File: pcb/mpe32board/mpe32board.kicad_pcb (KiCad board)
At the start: 4 copper layers, 98 x 79 mm, 160 parts, among them J1 Conn_ST_STDC14, J10 Conn_01x04, J11 Conn_01x04, J12 Conn_01x04, J13 Conn_01x04, J14 Conn_01x04, J15 Conn_01x04, J16 Conn_01x04, J17 Conn_01x04, J18 Conn_01x04, J19 Conn_01x04, J2 USB_C_Receptacle_USB2.0_16P, J20 Conn_01x04, J21 Conn_01x04, J22 Conn_01x04, J23 Conn_01x04, J24 Conn_01x04, J25 Conn_01x04, J26 Conn_01x04, J27 Conn_01x04, J3 Conn_01x01_Socket, J4 Conn_01x04, J44 Conn_01x05, J45 Conn_01x04_Socket, J46 Conn_02x10_Counter_Clockwise, J48 Micro_SD_Card_Det_Hirose_DM3AT, J49 AudioJack3_SwitchT, J5 Conn_01x04, J6 Conn_01x04, J7 Conn_01x04, J8 Conn_01x04, J9 Conn_01x04, SW1 SW_Push, SW2 SW_Push, SW3 SW_Push, SW4 SW_Push, SW5 SW_Push, SW6 SW_Push, U1 TAC5212IRGER, U10 W9812G6KH-75, U11 IP4252CZ16, U2 USBLC6-2P6, U3 AMS1117-3.3, U4 TCA9548ARGER, U5 TCA9548ARGER, U6 TCA9548ARGER, U9 STM32H743IITx

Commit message: silkscreen connectors
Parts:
- added kibuzzard-69FF710F: G***, kibuzzard-69FF710F, F.Cu at (145.6, 153.3)
- added kibuzzard-69FF713D: G***, kibuzzard-69FF713D, F.Cu at (153.5, 153.2)
- added kibuzzard-69FF7163: G***, kibuzzard-69FF7163, F.Cu at (145.6, 148.0)
- added kibuzzard-69FF7167: G***, kibuzzard-69FF7167, F.Cu at (153.5, 148.0)
- added kibuzzard-69FF7176: G***, kibuzzard-69FF7176, F.Cu at (145.6, 142.7)
- added kibuzzard-69FF717D: G***, kibuzzard-69FF717D, F.Cu at (153.5, 142.7)
- added kibuzzard-69FF7195: G***, kibuzzard-69FF7195, F.Cu at (145.6, 137.4)
- added kibuzzard-69FF719E: G***, kibuzzard-69FF719E, F.Cu at (153.5, 137.4)
- added kibuzzard-69FF71B5: G***, kibuzzard-69FF71B5, F.Cu at (145.6, 132.1)
- added kibuzzard-69FF71C5: G***, kibuzzard-69FF71C5, F.Cu at (153.5, 132.1)
- added kibuzzard-69FF71DB: G***, kibuzzard-69FF71DB, F.Cu at (153.5, 126.8)
- added kibuzzard-69FF71E0: G***, kibuzzard-69FF71E0, F.Cu at (145.6, 126.9)
- added kibuzzard-69FF72BF: G***, kibuzzard-69FF72BF, F.Cu at (145.6, 121.5)
- added kibuzzard-69FF72C5: G***, kibuzzard-69FF72C5, F.Cu at (153.5, 121.5)
- added kibuzzard-69FF72D8: G***, kibuzzard-69FF72D8, F.Cu at (145.6, 116.3)
- added kibuzzard-69FF72DF: G***, kibuzzard-69FF72DF, F.Cu at (153.5, 116.2)
- added kibuzzard-69FF72F7: G***, kibuzzard-69FF72F7, F.Cu at (145.6, 111.0)
- added kibuzzard-69FF72FD: G***, kibuzzard-69FF72FD, F.Cu at (153.5, 111.0)
- added kibuzzard-69FF730D: G***, kibuzzard-69FF730D, F.Cu at (145.6, 105.7)
- added kibuzzard-69FF7319: G***, kibuzzard-69FF7319, F.Cu at (153.5, 105.7)
- added kibuzzard-69FF7327: G***, kibuzzard-69FF7327, F.Cu at (145.6, 100.4)
- added kibuzzard-69FF732F: G***, kibuzzard-69FF732F, F.Cu at (153.5, 100.4)
- added kibuzzard-69FF7392: G***, kibuzzard-69FF7392, F.Cu at (145.6, 95.1)
- added kibuzzard-69FF73DD: G***, kibuzzard-69FF73DD, F.Cu at (153.5, 95.1)
- moved JP1 7.68 mm to (68.4, 118.8), turned to 180 degrees
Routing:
- net +5V: track 43.5 -> 54.0 mm
- net Net-(J45-Pin_3): track 5.17 -> 10.3 mm
- net 4_SD4: track 26.8 -> 28.2 mm
- net 2_SD2: track 34.2 -> 33.3 mm
- net 12_SD4: track 30.0 -> 29.1 mm
- net 19_SC3: track 33.0 -> 32.3 mm
- net 12_SC4: track 29.5 -> 28.8 mm
- net +3V3: track 331.4 -> 332.1 mm
- net 2_SC2: track 31.7 -> 32.4 mm
- net 8_SD0: track 32.1 -> 31.6 mm

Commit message: length match sdram
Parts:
- removed C1: 4.7μF, Capacitor_SMD:C_0603_1608Metric
- removed U11: IP4252CZ16, Package_SON:Nexperia_HUSON-16_USON-16-1EP_1.35x3.3mm_P0.4mm_EP0.4x2.8mm
- added C35: 100nF, Capacitor_SMD:C_0603_1608Metric, F.Cu at (89.0, 126.5)
- added C36: 100nF, Capacitor_SMD:C_0603_1608Metric, F.Cu at (89.0, 128.0)
- added C37: 100nF, Capacitor_SMD:C_0603_1608Metric, F.Cu at (89.0, 118.4)
- added C38: 100nF, Capacitor_SMD:C_0603_1608Metric, F.Cu at (89.0, 121.4)
- added C39: 100nF, Capacitor_SMD:C_0603_1608Metric, F.Cu at (83.8, 105.8)
- added C40: 100nF, Capacitor_SMD:C_0603_1608Metric, F.Cu at (69.4, 119.5)
- added C41: 100nF, Capacitor_SMD:C_0603_1608Metric, F.Cu at (69.5, 124.3)
- moved JP1 7.90 mm to (63.9, 125.3), turned to 90 degrees
- moved R21 7.15 mm to (93.1, 134.1), turned to -90 degrees
- moved R41 4.45 mm to (89.0, 102.8)
- moved R42 4.45 mm to (89.0, 104.2)
- moved C3 3.56 mm to (90.3, 107.1), turned to 135 degrees
- moved C11 2.37 mm to (89.0, 124.4)
- moved C15 2.37 mm to (89.0, 122.9)
- moved C2 0.86 mm to (89.8, 115.4)
- moved C10 0.78 mm to (89.0, 119.9)
- moved C8 0.67 mm to (121.4, 115.6)
- moved C31 0.57 mm to (76.7, 102.9)
- moved C32 0.57 mm to (76.7, 101.4)
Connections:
- J2 pad SH: GND -> (no net)
- J48 pad 1: Net-(J48-DAT2) -> SDMMC1_D2
- J48 pad 10: Net-(J48-DET_A) -> SDCARD_DET
- J48 pad 2: Net-(J48-DAT3/CD) -> SDMMC1_D3
- J48 pad 3: Net-(J48-CMD) -> SDMMC1_CMD
- J48 pad 5: Net-(J48-CLK) -> SDMMC1_CK
- J48 pad 7: Net-(J48-DAT0) -> SDMMC1_D0
- J48 pad 8: Net-(J48-DAT1) -> SDMMC1_D1
- J48 pad SH: GND -> (no net)
- U9 pad 100: BTN2_INTERNAL -> unconnected-(U9-PD12-Pad100)
- U9 pad 110: unconnected-(U9-PG6-Pad110) -> BTN1_INTERNAL
- U9 pad 111: unconnected-(U9-PG7-Pad111) -> BTN2_INTERNAL
- U9 pad 99: BTN1_INTERNAL -> unconnected-(U9-PD11-Pad99)
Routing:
- net FMC_SDNWE: track 22.1 -> 43.8 mm, vias 2 -> 4
- net I2C2_SDA: track 24.6 -> 5.18 mm, vias 2 -> 0
- net Net-(J48-DET_A): track 15.9 -> 0.00 mm
- net SDMMC1_D2: track 53.5 -> 68.2 mm
- net Net-(J48-DAT2): track 13.3 -> 0.00 mm
- net SDMMC1_D3: track 53.1 -> 66.3 mm
- net Net-(J48-DAT3/CD): track 12.0 -> 0.00 mm
- net +3V3: track 332.1 -> 343.7 mm
- net SDMMC1_CMD: track 53.8 -> 65.1 mm
- net Net-(J48-CMD): track 10.5 -> 0.00 mm
- net Net-(J45-Pin_3): track 10.3 -> 0.00 mm
- net FMC_SDNE0: track 26.8 -> 37.0 mm, vias 2 -> 4
- net SDMMC1_CK: track 53.9 -> 63.2 mm
- net GND: track 283.0 -> 274.3 mm, vias 91 -> 94
- net Net-(J48-CLK): track 8.26 -> 0.00 mm
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
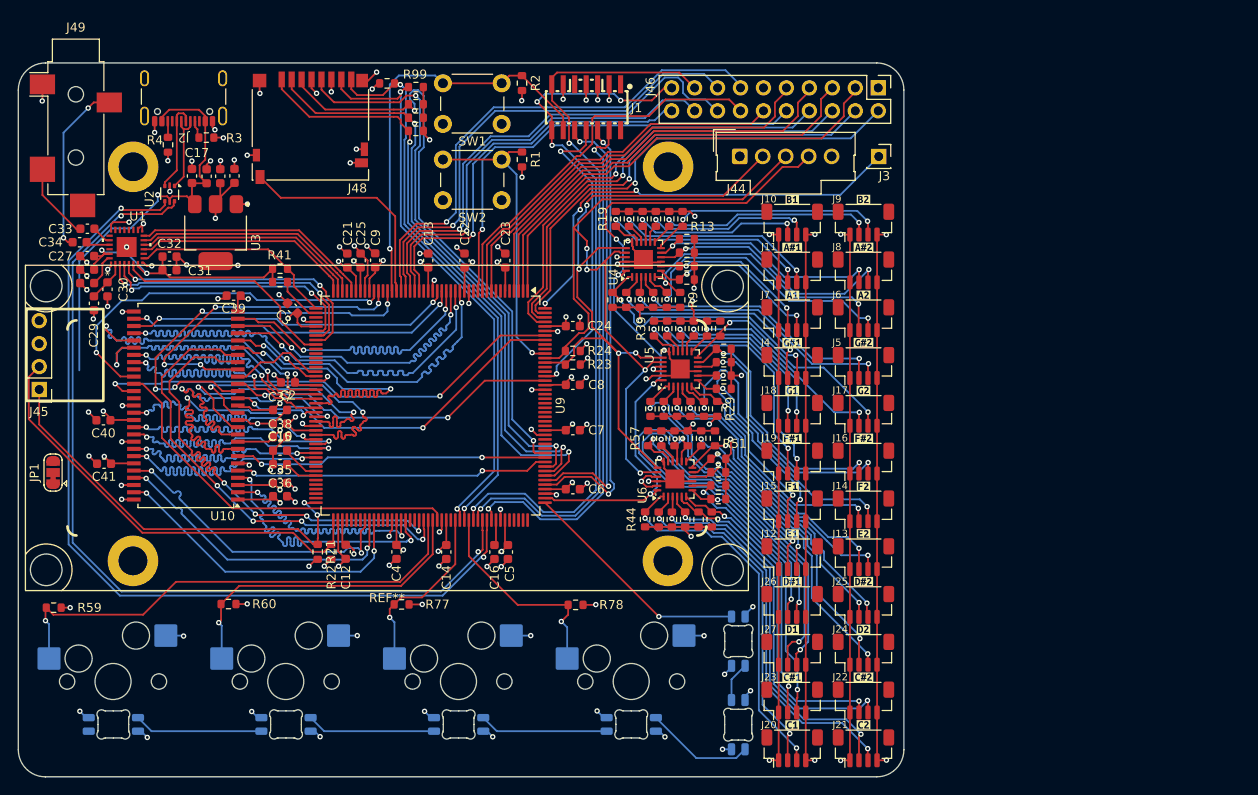
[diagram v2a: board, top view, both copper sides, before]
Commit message: drc checks n more
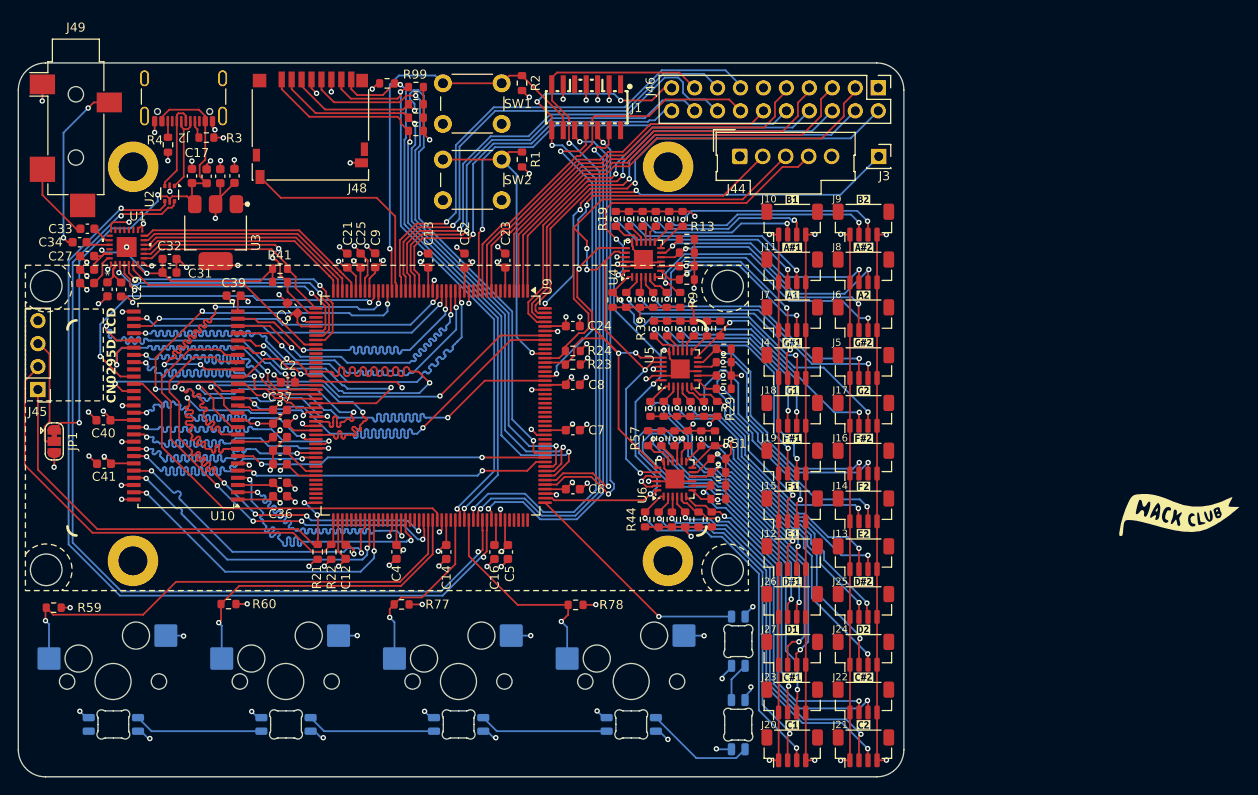
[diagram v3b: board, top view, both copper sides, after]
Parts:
- added G***: LOGO, 1_udu_lib:hackclub, F.Cu at (188.3, 130.3)
- CN0295D LCD: renamed from REF**
- moved JP1 3.45 mm to (64.0, 121.9), turned to -90 degrees
- moved C29 3.38 mm to (71.4, 105.1)
- moved C31 0.27 mm to (76.7, 103.2)
- moved C32 0.27 mm to (76.7, 101.7)
- moved J45 0.14 mm to (62.2, 116.1)
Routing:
- net FMC_SDNRAS: track 10.6 -> 47.2 mm, vias 0 -> 2
- net I2C2_SDA: track 5.18 -> 25.5 mm, vias 0 -> 2
- net FMC_NBL0: track 39.6 -> 52.9 mm
- net Net-(J45-Pin_3): track 0.00 -> 12.5 mm
- net FMC_SDNCAS: track 37.3 -> 47.1 mm
- net +5V: track 47.4 -> 56.2 mm, vias 1 -> 2
- net FMC_A10: track 36.5 -> 28.1 mm
- net FMC_SDNE0: track 37.0 -> 43.8 mm
- net GND: track 274.3 -> 279.8 mm, vias 94 -> 90
- net I2C4_SDA: track 49.0 -> 52.6 mm
- net +3V3: track 343.7 -> 346.9 mm, vias 62 -> 63
- net I2C4_SCL: track 46.8 -> 49.9 mm
- net I2S1_SDO: track 25.1 -> 24.3 mm
- net FMC_SDCKE0: track 41.8 -> 41.1 mm
- net AVDD: track 30.4 -> 31.0 mm
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
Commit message: silkscreen for main board + finished sensor board
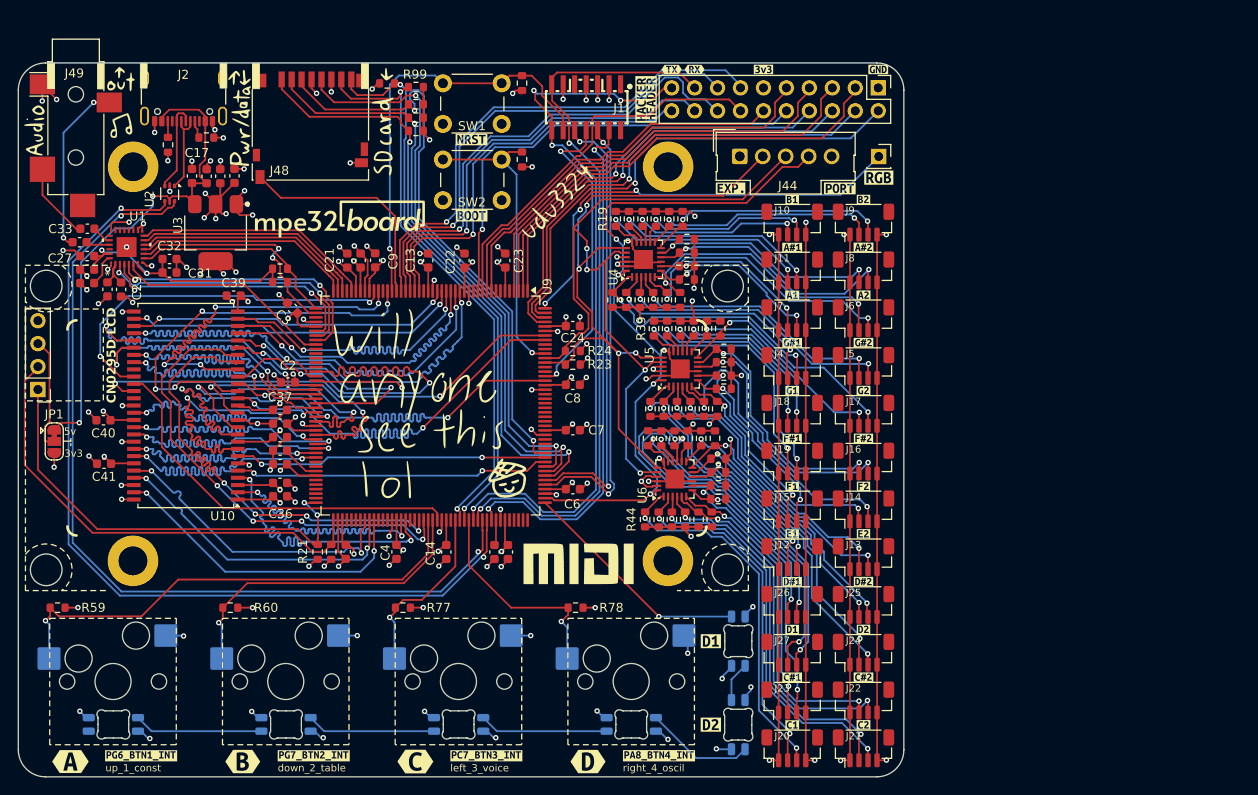
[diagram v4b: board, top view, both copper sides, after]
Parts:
- added G***: LOGO, 1_udu_lib:card_nfc_icon, F.Cu at (114.1, 125.9)
- added G***: LOGO, 1_udu_lib:mpe32board_f_silk, F.Cu at (108.3, 119.1)
- added G***: LOGO, 1_udu_lib:mpe32board_logo_sm_sm_lg, F.Cu at (95.5, 97.3)
- added G***: LOGO, 1_udu_lib:card_nfc_icon, B.Cu at (66.2, 86.9)
- added G***: LOGO, 1_udu_lib:mpe32board_b_silk, B.Cu at (108.6, 118.3)
- added G***: LOGO, 1_udu_lib:missing_image, B.Cu at (110.3, 87.4)
- added G***: LOGO, 1_udu_lib:mpe32board_logo_sm, B.Cu at (150.6, 119.8)
- added REF**: Screw_Generic_2.0x3.0mm_SilkScreen, Symbol:Screw_Generic_2.0x3.0mm_SilkScreen, B.Cu at (69.0, 131.8)
- added REF**: Screw_Generic_2.0x3.0mm_SilkScreen, Symbol:Screw_Generic_2.0x3.0mm_SilkScreen, B.Cu at (69.8, 88.1)
- added REF**: Screw_Generic_2.0x3.0mm_SilkScreen, Symbol:Screw_Generic_2.0x3.0mm_SilkScreen, B.Cu at (127.9, 131.8)
- added REF**: KiCad-Logo_8mm_SilkScreen, Symbol:KiCad-Logo_8mm_SilkScreen, B.Cu at (84.7, 99.2)
- added REF**: Screw_Generic_2.0x3.0mm_SilkScreen, Symbol:Screw_Generic_2.0x3.0mm_SilkScreen, B.Cu at (128.6, 88.1)
- added kibuzzard-6A06ADD4: G***, kibuzzard-6A06ADD4, F.Cu at (84.8, 157.3)
- added kibuzzard-6A06ADDB: G***, kibuzzard-6A06ADDB, F.Cu at (103.9, 157.3)
- added kibuzzard-6A06ADE0: G***, kibuzzard-6A06ADE0, F.Cu at (123.0, 157.3)
- added kibuzzard-6A06B0BE: G***, kibuzzard-6A06B0BE, F.Cu at (111.8, 156.7)
- added kibuzzard-6A06B0F2: G***, kibuzzard-6A06B0F2, F.Cu at (73.6, 156.7)
- added kibuzzard-6A06B118: G***, kibuzzard-6A06B118, F.Cu at (92.7, 156.7)
- added kibuzzard-6A06B135: G***, kibuzzard-6A06B135, F.Cu at (130.9, 156.7)
- added kibuzzard-6A06B367: G***, kibuzzard-6A06B367, F.Cu at (136.6, 144.0)
- added kibuzzard-6A06B37C: G***, kibuzzard-6A06B37C, F.Cu at (136.6, 153.2)
- added kibuzzard-6A0925D0: G***, kibuzzard-6A0925D0, F.Cu at (65.8, 157.3)
- added kibuzzard-6A0A0E58: G***, kibuzzard-6A0A0E58, F.Cu at (142.5, 80.7)
- added kibuzzard-6A0A0E61: G***, kibuzzard-6A0A0E61, F.Cu at (155.2, 80.7)
- added kibuzzard-6A0A0E69: G***, kibuzzard-6A0A0E69, F.Cu at (134.8, 80.7)
- added kibuzzard-6A0A0E77: G***, kibuzzard-6A0A0E77, F.Cu at (132.3, 80.7)
- added kibuzzard-6A0A0F62: G***, kibuzzard-6A0A0F62, F.Cu at (155.2, 92.7)
- added kibuzzard-6A0A0F87: G***, kibuzzard-6A0A0F87, F.Cu at (150.9, 93.9)
- added kibuzzard-6A0A106B: G***, kibuzzard-6A0A106B, F.Cu at (110.2, 96.9)
- added kibuzzard-6A0A1170: G***, kibuzzard-6A0A1170, F.Cu at (138.8, 93.9)
- added kibuzzard-6A0A124F: G***, kibuzzard-6A0A124F, F.Cu at (129.5, 84.0)
- added kibuzzard-6A0A127D: G***, kibuzzard-6A0A127D, F.Cu at (110.2, 88.5)
- G***: moved to B.Cu
- moved G*** 104.7 mm to (92.9, 87.0), turned to 180 degrees
- moved R60 0.45 mm to (83.5, 140.3)
- moved R59 0.43 mm to (64.3, 140.3)
- moved R77 0.39 mm to (102.6, 140.3)
- moved R78 0.31 mm to (121.7, 140.3)
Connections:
- J46 pad 1: +3V3 -> GND
- J46 pad 11: GND -> +3V3
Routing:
- net +3V3: track 346.9 -> 356.4 mm, vias 63 -> 68
- net GND: track 279.8 -> 289.0 mm, vias 90 -> 93
- net LPUART1_TX: track 79.8 -> 81.4 mm
- net NRST: track 46.6 -> 47.2 mm
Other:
- board text added: "3v3"
- board text added: "5v"
- board text added: "down_2_table"
- board text added: "left_3_voice"
- board text added: "missing.png"
- board text added: "right_4_oscil"
- board text added: "up_1_const"
